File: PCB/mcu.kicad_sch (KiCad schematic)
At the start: 33 parts, among them J6 Conn_01x02, J8 Conn_01x02, SW1 Boot, SW2 Reset, U6 ESP32-C3FH4X, Y1 40MHz

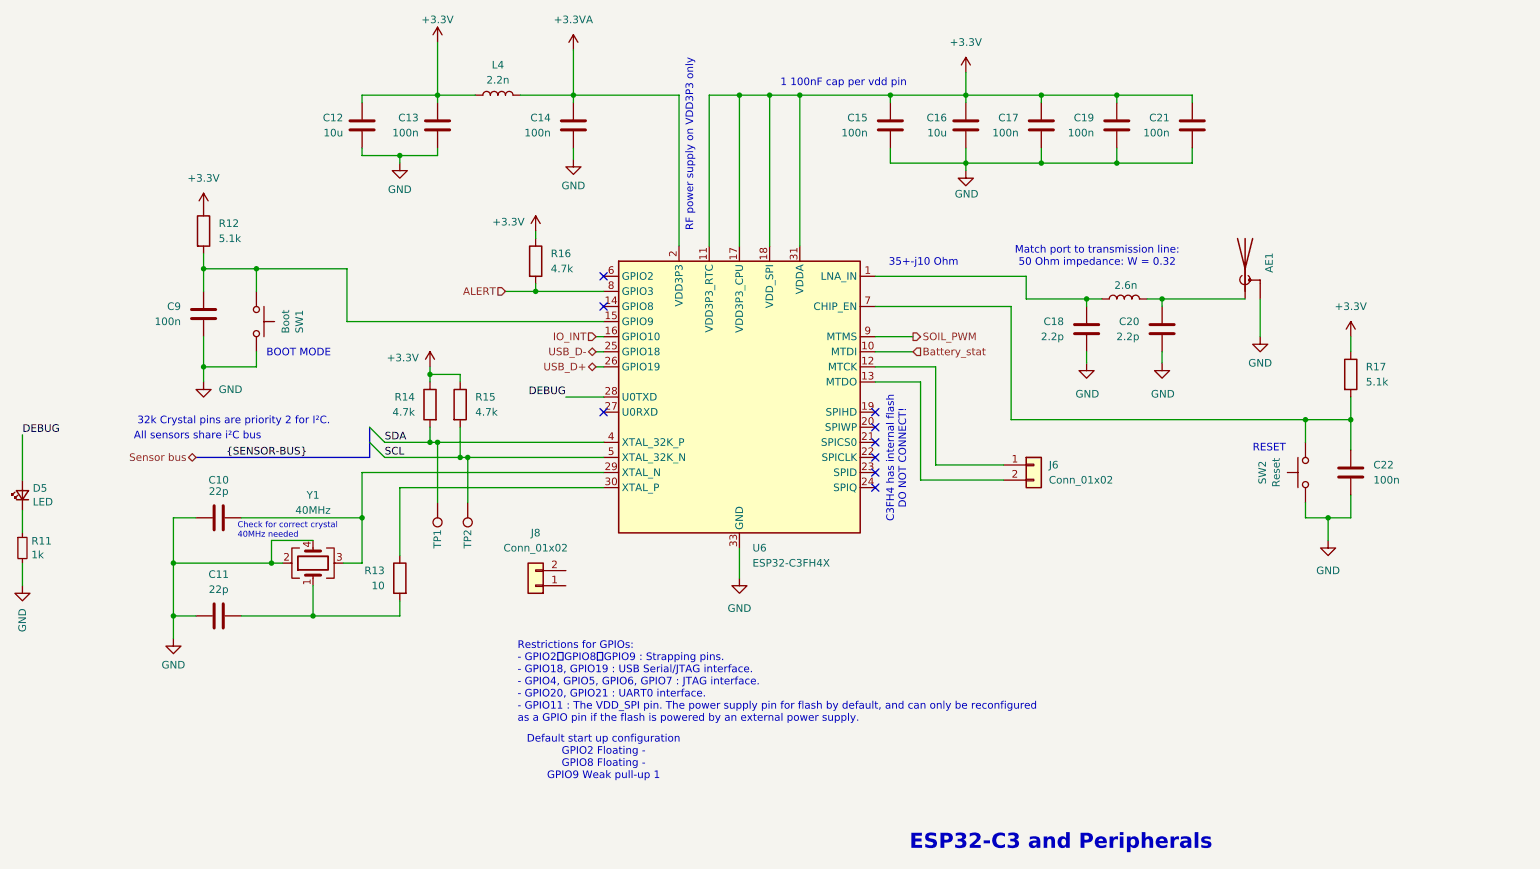
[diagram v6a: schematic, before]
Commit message: ESD protection and Boost UVLO
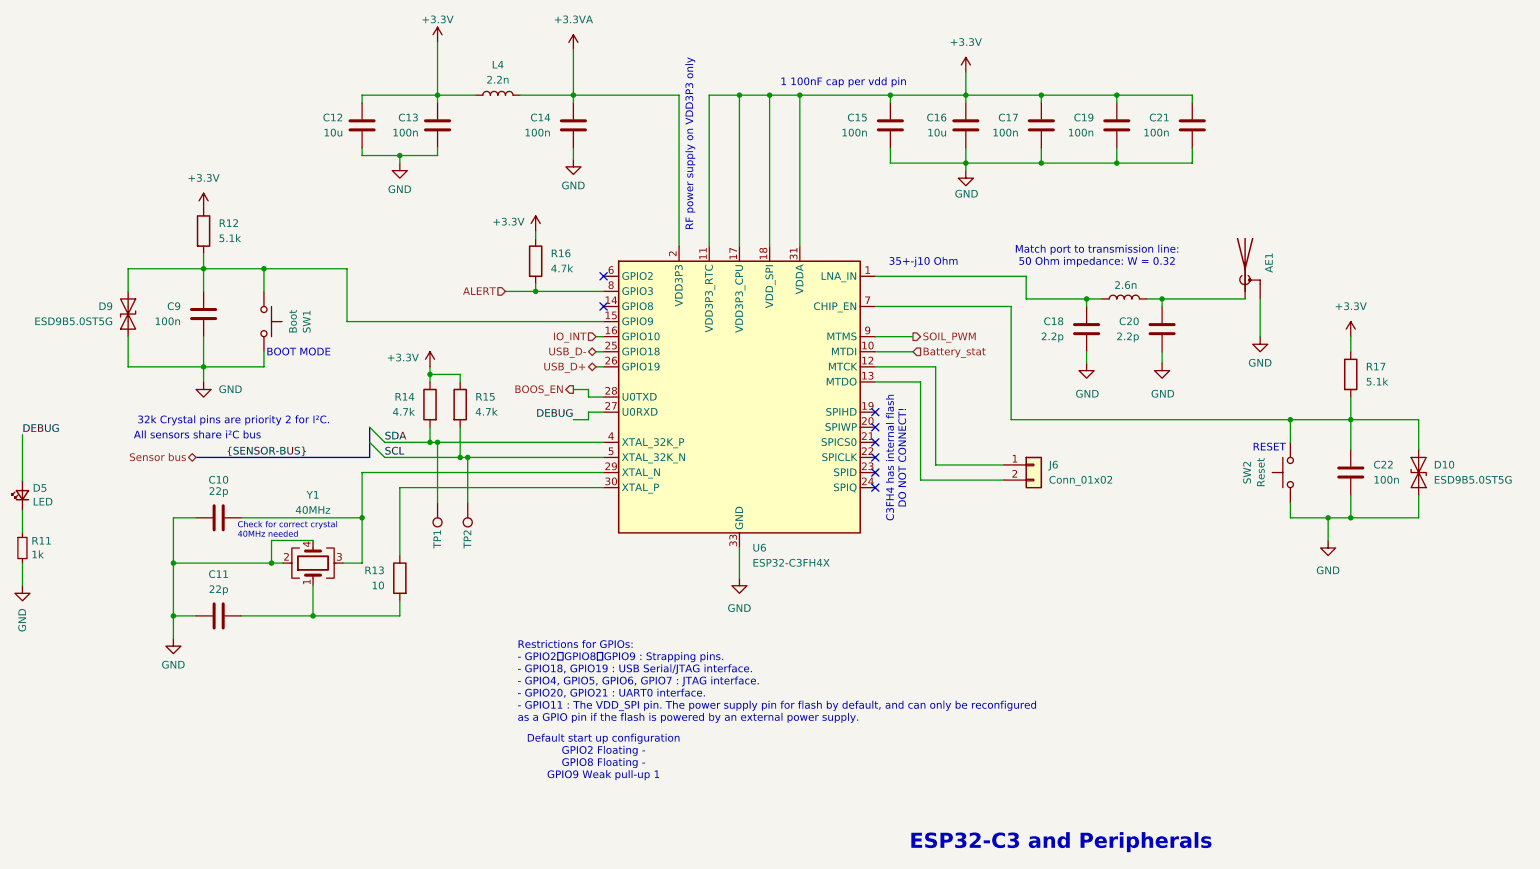
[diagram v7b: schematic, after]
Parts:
- removed J8: Conn_01x02, Connector_PinHeader_2.54mm:PinHeader_1x02_P2.54mm_Vertical, symbol Connector_Generic:Conn_01x02
- added D10, D9: ESD9B5.0ST5G, Diode_SMD:D_SOD-923, symbol Diode:ESD9B5.0ST5G
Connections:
- net DEBUG: now also U6.27 (U0RXD); no longer U6.28 (U0TXD)
- net GND: now also D10.1 (A1), D9.1 (A1)
- net at C22.1, R17.2, SW2.1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: now also D10.2 (A2)
- net at C9.2, R12.2, SW1.1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: now also D9.2 (A2)
- new net BOOS_EN: U6.28 (U0TXD)
- no-connect marks 9 -> 8
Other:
- moved on the sheet: SW1, SW2

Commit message: Production files
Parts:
- C10, C11: value 22p -> 15p
- R11: LCSC C163928 -> (none)
- R14, R15, R16: value 4.7k -> 5.1k
- renumbered D5 to D6, D9 to D7, D10 to D8
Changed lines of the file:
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@@
 			)
 		)
-		(property "LCSC" "C163928"
+		(property "LCSC" ""
 			(at 30.48 124.46 0)
 			(effects
@@
 			)
 		)
-		(property "Value" "22p"
+		(property "Value" "15p"
 			(at 63.5 131.445 90)
 			(effects
@@
 			)
 		)
-		(property "Value" "4.7k"
+		(property "Value" "5.1k"
 			(at 119.38 77.4699 0)
 			(effects
@@
 			)
 		)
-		(property "Value" "4.7k"
+		(property "Value" "5.1k"
 			(at 106.68 101.5999 0)
 			(effects
@@
 		(on_board yes)
 		(dnp no)
-		(property "Reference" "D5"
+		(property "Reference" "D6"
 			(at 32.2072 114.4016 90)
 			(effects
@@
 			(project "Plant-health-meter"
 				(path "/357055bf-c309-4d6b-a2fa-f5ee5ba59771/f878f43f-0ef0-4ca5-9286-ff16b4b716af"
-					(reference "D5")
+					(reference "D6")
 					(unit 1)
 				)
@@
 		(on_board yes)
 		(dnp no)
-		(property "Reference" "D10"
+		(property "Reference" "D8"
 			(at 267.97 110.4899 90)
 			(effects
@@
 			(project "Plant-health-meter"
 				(path "/357055bf-c309-4d6b-a2fa-f5ee5ba59771/f878f43f-0ef0-4ca5-9286-ff16b4b716af"
-					(reference "D10")
+					(reference "D8")
 					(unit 1)
 				)
@@
 			)
 		)
-		(property "Value" "4.7k"
+		(property "Value" "5.1k"
 			(at 96.52 101.5999 0)
 			(effects
@@
 			)
 		)
-		(property "Value" "22p"
+		(property "Value" "15p"
 			(at 63.5 114.935 90)
 			(effects
@@
 		(on_board yes)
 		(dnp no)
-		(property "Reference" "D9"
+		(property "Reference" "D7"
 			(at 45.72 83.8199 90)
 			(effects
@@
 			(project "Plant-health-meter"
 				(path "/357055bf-c309-4d6b-a2fa-f5ee5ba59771/f878f43f-0ef0-4ca5-9286-ff16b4b716af"
-					(reference "D9")
+					(reference "D7")
 					(unit 1)
 				)
